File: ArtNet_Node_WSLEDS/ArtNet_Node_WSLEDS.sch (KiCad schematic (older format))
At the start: 59 parts, among them J1 Conn_01x02_Female, J2 Conn_01x04_Female, J3 Conn_01x03_Male, J4 Conn_01x08_Male, J5 Conn_01x08_Male, Q1 BSS138, Q2 BSS138, Q3 BSS138, Q4 BSS138, Q5 BSS138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

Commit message: Update the PCB design;
Migration to FastLED library (more reliable). And 4 more outputs which makes is 12 in total (+1 if soldered to R14).
Also change the output driver to 74HCT245. The mosfet solution was not working very on fast speeds.
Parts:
- removed Q1, Q2, Q3, Q4, Q5, Q6, Q7, Q8: BSS138, TO_SOT_Packages_SMD:SOT-23, symbol Transistor_FET:BSS138
- removed R15, R16, R17, R20, R21, R22, R23: 10k, Resistors_SMD:R_1206_HandSoldering, symbol Device:R
- removed R18, R19, R24, R25: 100R, Resistors_SMD:R_1206_HandSoldering, symbol Device:R
- added J6: Conn_01x08_Male, TerminalBlocks_Phoenix:TerminalBlock_Phoenix_MPT-2.54mm_8pol, symbol Connector:Conn_01x08_Male
- added U6, U7: 74HCT245, Housings_SOIC:SO-20_12.8x7.5mm_Pitch1.27mm, symbol 74xx:74HC245
- R14, R2, R3, R4, R5, R6, R7, R8, R9: value 10k -> 100R
- U4, U5: footprint TO_SOT_Packages_SMD:SOT-223 -> TO_SOT_Packages_SMD:SOT-223-3_TabPin2
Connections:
- net +12V: now also JP1.3 (B); no longer C4.1, JP1.1 (A), R6.2, R7.2, R8.2, R9.2, U5.1 (VI)
- net +3V3: no longer R14.2, R2.2, R3.2, R4.2, R5.2
- net +5V: now also C4.1, JP1.2 (C), U5.1 (VI), U6.1 (A->B), U6.20 (VCC), U7.1 (A->B), U7.20 (VCC); no longer JP1.3 (B)
- net FrameSync: now also U2.24 (17_A3_SDA0_Touch); no longer U2.3 (1_TX1_Touch)
- net GND: now also U2.17 (GND), J6.2 (Pin_2), J6.4 (Pin_4), J6.6 (Pin_6), J6.8 (Pin_8), U6.10 (GND), U6.19 (CE), U7.10 (GND), U7.19 (CE), U7.7 (A5), U7.8 (A6), U7.9 (A7)
- net HAPPY: now also U2.21 (14_A0_SCK); no longer U2.29 (22_A8_Touch_PWM)
- net LED1: now also U2.19 (A14/DAC), U6.2 (A0); no longer R2.1, U2.4 (2)
- net LED1_OUT: now also R2.1; no longer R10.1
- net LED2: now also U2.12 (10_TX2_CS_PWM), U6.3 (A1); no longer R3.1, U2.19 (A14/DAC)
- net LED2_OUT: now also R6.1; no longer R11.1
- net LED3: now also U2.11 (9_RX2_CS_PWM), U6.4 (A2); no longer R4.1, U2.9 (7_RX3_DOUT)
- net LED3_OUT: now also R3.1; no longer R12.1
- net LED4: now also U6.5 (A3); no longer R5.1
- net LED4_OUT: now also R7.1; no longer R13.1
- net LED5: now also U2.9 (7_RX3_DOUT), U6.6 (A4); no longer R14.1, U2.8 (6_PWM)
- net LED5_OUT: now also R4.1
- net LED6: now also U2.8 (6_PWM), U6.7 (A5); no longer U2.27 (20_A6_CS_PWM)
- net LED6_OUT: now also R8.1
- net LED7: now also U2.7 (5_TX1_PWM), U6.8 (A6); no longer U2.28 (21_A7_RX1_CS_PWM)
- net LED7_OUT: now also R5.1
- net LED8: now also U2.4 (2), U6.9 (A7); no longer U2.7 (5_TX1_PWM)
- net LED8_OUT: now also R9.1
- net WIZ_RESET: now reaches R28.1, U3.3 (~MR)
- net WIZ_RESET: now also U2.3 (1_TX1_Touch)
- net at R10.2: now also U7.18 (B0); no longer R6.1
- net LED9: now reaches U2.22 (15_A1_CS_Touch)
- net LED9: now also U7.2 (A0)
- net LED13: now reaches U2.30 (23_A9_Touch_PWM)
- net LED13: now also U7.6 (A4)
- net at R11.2: now also U7.16 (B2); no longer R7.1
- net at R12.2: now also U7.17 (B1); no longer R8.1
- net at R13.2: now also U7.15 (B3); no longer R9.1
- net at J1.1 (Pin_1): now also JP1.1 (A); no longer JP1.2 (C)
- new net: R2.2, U6.18 (B0)
- new net: R6.2, U6.17 (B1)
- new net: R3.2, U6.16 (B2)
- new net: R7.2, U6.15 (B3)
- new net: R4.2, U6.14 (B4)
- new net: R8.2, U6.13 (B5)
- new net: R5.2, U6.12 (B6)
- new net: R9.2, U6.11 (B7)
- new net: R14.2, U7.14 (B4)
- new net LED10: U2.27 (20_A6_CS_PWM), U7.3 (A1)
- new net LED10_OUT: J6.3 (Pin_3), R12.1
- new net LED11: U2.28 (21_A7_RX1_CS_PWM), U7.4 (A2)
- new net LED11_OUT: J6.5 (Pin_5), R11.1
- new net LED12: U2.29 (22_A8_Touch_PWM), U7.5 (A3)
- new net LED12_OUT: J6.7 (Pin_7), R13.1
- new net LED9_OUT: J6.1 (Pin_1), R10.1
- no-connect marks 31 -> 28
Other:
- moved on the sheet: C1, D1, J1, J4, J5, JP1, R1, R27, U1

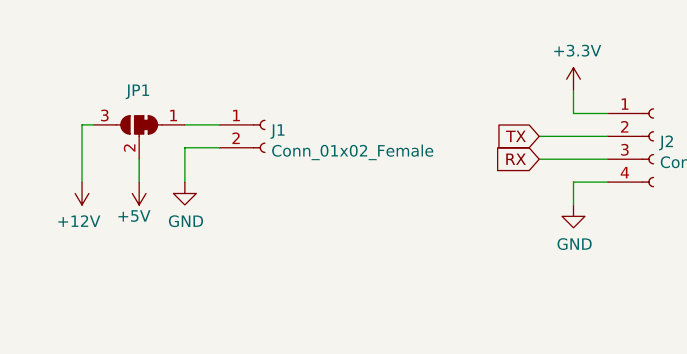
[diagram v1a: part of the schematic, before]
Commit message: Update ArtNet_Node_WSLEDS.sch
Added a schematic remark
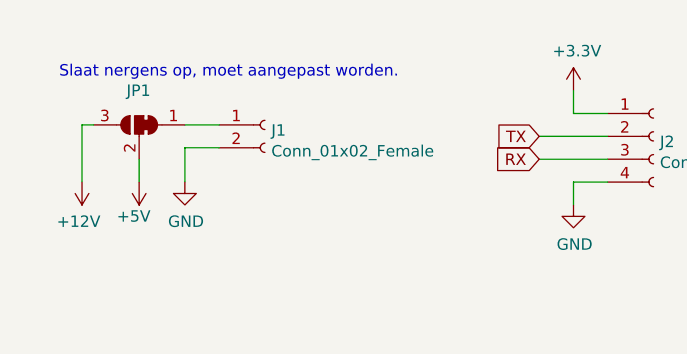
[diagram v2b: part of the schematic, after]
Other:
- note added: "Slaat nergens op, moet aangepast worden."
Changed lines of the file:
@@
 Wire Wire Line
 	4200 4250 4350 4250
+Text Notes 750  800  0    50   ~ 0
+Slaat nergens op, moet aangepast worden.
 $EndSCHEMATC
